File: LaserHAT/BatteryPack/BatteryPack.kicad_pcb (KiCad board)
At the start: 2 copper layers, 100 x 100 mm, 144 parts, among them J1 TYPE-C-31-M-12, J3 B4B-PH-K-S(LF)(SN), J5 S5B-XH-A-1(LF)(SN), J6 S5B-XH-A-1(LF)(SN), J7 XT60PW-M, J8 XT60PW-M, Q1 AO3401A, Q10 AO3400A, Q11 AO3400A, Q12 AO3400A, Q13 AO3401A, Q14 AO3400A, Q15 AO3400A, Q16 AO3400A, Q17 AO3400A, Q18 AO3400A, Q6 AO3401A, Q7 AO3400A, Q8 AO3400A, Q9 AO3400A, SW1 CAX-MTS203M-YB-10.6JL, U1 LM393DR2G, U10 HY2213-BB3A, U11 HY2213-BB3A, U12 HY2213-BB3A, U13 HY2213-BB3A, U14 LM393DR2G, U15 LM393DR2G, U16 CJ431, U2 LM393DR2G, U3 CJ431, U4 CH224A, U5 CN3704, U6 HY2213-BB3A, U7 HY2213-BB3A, U8 HY2213-BB3A, U9 HY2213-BB3A

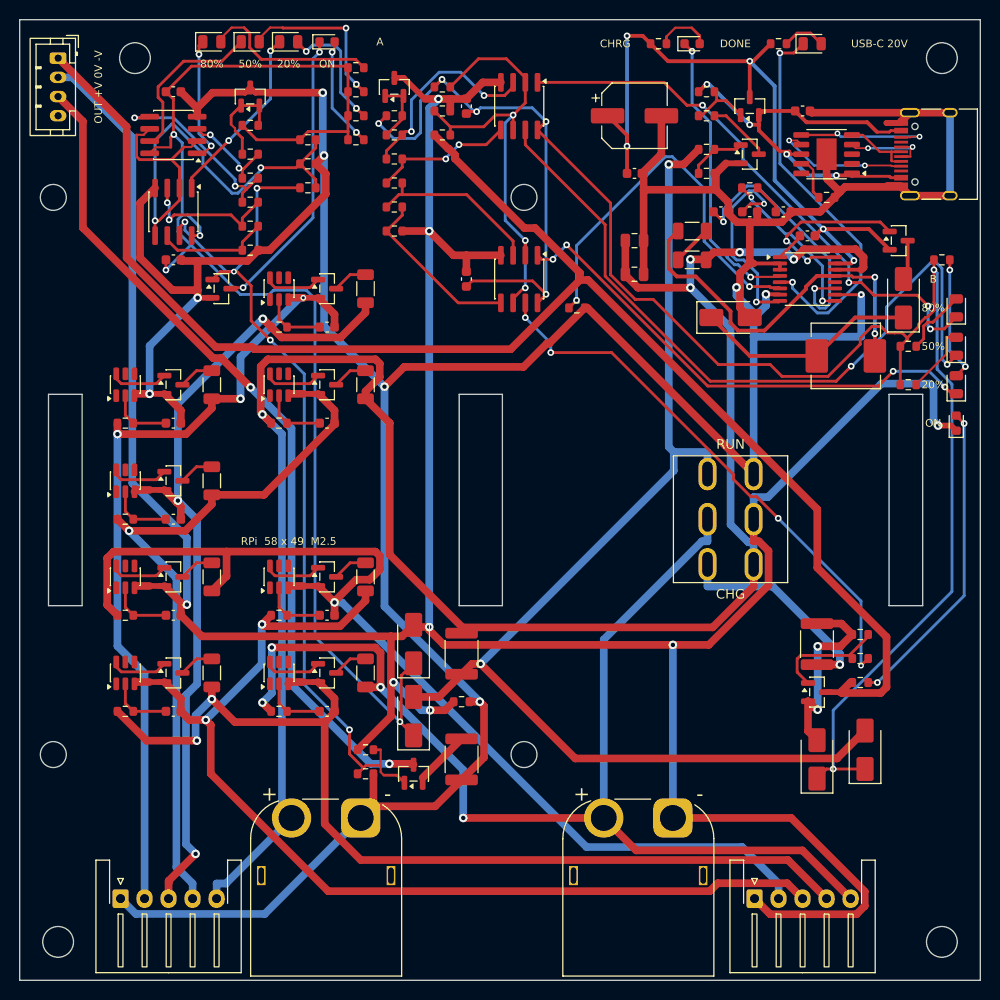
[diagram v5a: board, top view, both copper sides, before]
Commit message: BatteryPack rev D: packs in series, floating charger switched between them by a relay under an STM32F042, ON/OFF toggle, plug interlock, 0V pour
Rev C's parallel/series toggle made half the board jump by a pack voltage, needed a PTC link and an equalising rule, and left no single
reference.  Rev D keeps the packs in series for good (GND / 0V / +BATB), floats the whole charger on its own ground CGND and lets an
HFD2 relay under an STM32F042F4P6 (USB DFU, firmware/) connect it to pack A or pack B: "charge the lower pack" in 3-minute slots with
the CN3704 power-cycled at every reconnection, per-pack CHG / DONE LEDs.  MTS-202 ON/OFF toggle; +V is enabled only with the module's
plug in (J3 pin 4 strapped to 0V) because the module dies from +V / -V without 0V; an EL817 opto turns the outputs off while a brick
is in.  Gauge rails through P-FETs, ladder re-tuned for the undropped rail.

Layout mirror-symmetric about x = 50 with the Pi along the top edge (its USB-C / HDMI face flush, module over the top-right corner
above J3), the gauge LED columns paired in the centre (80 / 50 / 20 / ON / CHG / DONE), toggle and USB-C in the middle of the front,
relay front-right, PD sink front-left, charger island in the centre column under the Pi.  Freerouting + maze_route; back-side 0V
pour; DRC 0/0/0, path / sync 0, lcsc_check clean, fab outputs and renders regenerated.  Firmware compiles only with an ARM toolchain
(not present here); DFU on the TSSOP-20 and the relay's pick-up at 20 V are first-board checks (README).

Co-Authored-By: Claude Fable 5.1 <noreply@anthropic.com>
Claude-Session: https://claude.ai/code/session_018vgLizGzYPynnY93ajvoVA
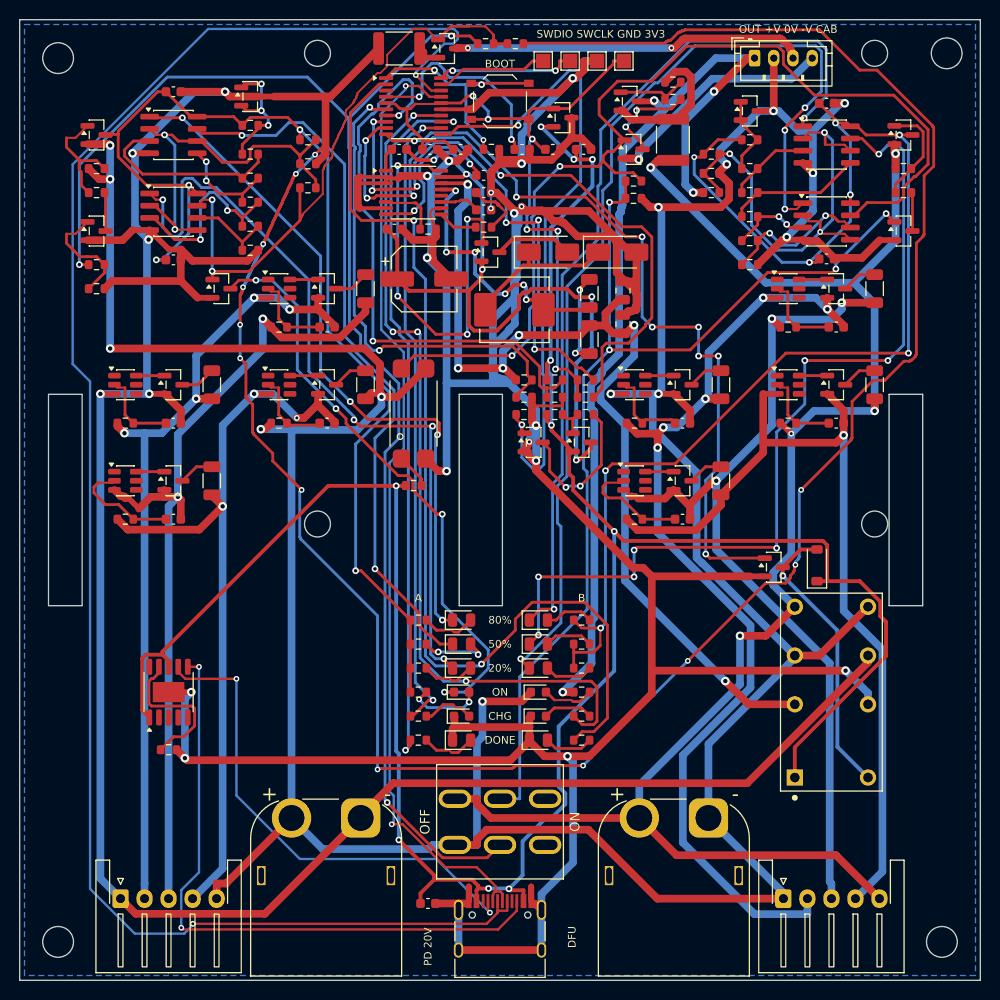
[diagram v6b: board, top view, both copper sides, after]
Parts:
- removed D15, D16, D5, D6: SS14, Diode_SMD:D_SMA
- removed F3: MF-MSMF110/24X-2, Fuse:Fuse_1812_4532Metric
- removed R30: 1M, Resistor_SMD:R_0603_1608Metric
- removed R41: 100k, Resistor_SMD:R_0603_1608Metric
- added C22: 1u, Capacitor_SMD:C_0603_1608Metric, F.Cu at (58.7, 13.5)
- added C23: 1u, Capacitor_SMD:C_0603_1608Metric, F.Cu at (55.5, 13.5)
- added C24: 100n, Capacitor_SMD:C_0603_1608Metric, F.Cu at (42.7, 13.5)
- added C25: 100n, Capacitor_SMD:C_0603_1608Metric, F.Cu at (45.9, 13.5)
- added C26: 100n, Capacitor_SMD:C_0603_1608Metric, F.Cu at (52.3, 13.5)
- added D17: KT-0603R, LED_SMD:LED_0603_1608Metric, F.Cu at (54.0, 72.5)
- added D18: KT-0805G, LED_SMD:LED_0805_2012Metric, F.Cu at (54.0, 75.0)
- added D19: 1N4148W, Diode_SMD:D_SOD-123, F.Cu at (83.0, 56.8)
- added K1: HFD2/024-M, battpack:Relay_HFD2, F.Cu at (84.5, 70.0)
- added Q19: 2N7002, Package_TO_SOT_SMD:SOT-23, F.Cu at (78.5, 57.0)
- added Q20: AO3401A, Package_TO_SOT_SMD:SOT-23, F.Cu at (8.00, 12.0)
- added Q21: 2N7002, Package_TO_SOT_SMD:SOT-23, F.Cu at (8.00, 22.0)
- added Q22: 2N7002, Package_TO_SOT_SMD:SOT-23, F.Cu at (63.9, 13.5)
- added Q23: AO3401A, Package_TO_SOT_SMD:SOT-23, F.Cu at (92.0, 12.0)
- added Q24: 2N7002, Package_TO_SOT_SMD:SOT-23, F.Cu at (92.0, 22.0)
- added R66: 1k, Resistor_SMD:R_0603_1608Metric, F.Cu at (41.5, 72.5)
- added R67: 470, Resistor_SMD:R_0603_1608Metric, F.Cu at (41.5, 75.0)
- added R68: 1k, Resistor_SMD:R_0603_1608Metric, F.Cu at (58.5, 72.5)
- added R69: 470, Resistor_SMD:R_0603_1608Metric, F.Cu at (58.5, 75.0)
- added R70: 10k, Resistor_SMD:R_0603_1608Metric, F.Cu at (49.1, 13.5)
- added R71: 100k, Resistor_SMD:R_0603_1608Metric, F.Cu at (52.5, 37.5)
- added R72: 18k, Resistor_SMD:R_0603_1608Metric, F.Cu at (52.5, 39.3)
- added R73: 100k, Resistor_SMD:R_0603_1608Metric, F.Cu at (55.7, 37.5)
- added R74: 18k, Resistor_SMD:R_0603_1608Metric, F.Cu at (55.7, 39.3)
- added R76: 10k, Resistor_SMD:R_0603_1608Metric, F.Cu at (41.0, 48.5)
- added R77: 100k, Resistor_SMD:R_0603_1608Metric, F.Cu at (8.00, 15.5)
- added R78: 100k, Resistor_SMD:R_0603_1608Metric, F.Cu at (8.00, 18.0)
- added R79: 100k, Resistor_SMD:R_0603_1608Metric, F.Cu at (8.00, 25.5)
- added R80: 100k, Resistor_SMD:R_0603_1608Metric, F.Cu at (8.00, 28.0)
- added R81: 1M, Resistor_SMD:R_0603_1608Metric, F.Cu at (63.9, 16.8)
- added R82: 1M, Resistor_SMD:R_0603_1608Metric, F.Cu at (63.9, 18.6)
- added R83: 100k, Resistor_SMD:R_0603_1608Metric, F.Cu at (92.0, 15.5)
- added R84: 100k, Resistor_SMD:R_0603_1608Metric, F.Cu at (92.0, 18.0)
- added SW2: TS-1187A-B-A-B, Button_Switch_SMD:SW_Push_1P1T_XKB_TS-1187A, F.Cu at (50.0, 8.50)
- added TP1: SWDIO, TestPoint:TestPoint_Pad_1.5x1.5mm, F.Cu at (54.5, 4.30)
- added TP2: SWCLK, TestPoint:TestPoint_Pad_1.5x1.5mm, F.Cu at (57.3, 4.30)
- added TP3: CGND, TestPoint:TestPoint_Pad_1.5x1.5mm, F.Cu at (60.1, 4.30)
- added TP4: +3V3, TestPoint:TestPoint_Pad_1.5x1.5mm, F.Cu at (62.9, 4.30)
- added U17: EL817S1(C)(TU)-F, battpack:EL817S1, F.Cu at (41.0, 41.0)
- added U18: TLV76033DBZR, Package_TO_SOT_SMD:SOT-23, F.Cu at (56.5, 10.2)
- added U19: STM32F042F4P6, Package_SO:TSSOP-20_4.4x6.5mm_P0.65mm, F.Cu at (41.0, 9.00)
- Q12: value AO3400A -> 2N7002
- R28, R29: value 15k -> 10k
- R4, R46: value 6.8k -> 6.2k
- SW1: value CAX-MTS203M-YB-10.6JL -> CAX-MTS202B2-BB-20.5JL; footprint battpack:SW_MTS-203 -> battpack:SW_MTS-202
- moved J1 93.7 mm to (50.0, 95.8), turned to 0 degrees
- moved C3 91.3 mm to (42.5, 92.0)
- moved R24 89.4 mm to (15.5, 76.0)
- moved U4 88.5 mm to (15.5, 70.0), turned to 90 degrees
- moved H7 86.8 mm to (89.0, 3.50)
- moved D10 81.2 mm to (46.0, 75.0)
- moved H8 78.0 mm to (31.0, 3.50)
- moved R40 77.6 mm to (51.6, 2.50)
- moved Q11 75.6 mm to (44.5, 3.00), turned to 0 degrees
- moved R39 74.6 mm to (48.5, 2.50)
- moved F2 74.3 mm to (39.5, 3.00), turned to 0 degrees
- moved D9 74.0 mm to (46.0, 72.5)
- moved J3 72.5 mm to (76.5, 4.00), turned to 0 degrees
- moved D1 69.1 mm to (46.0, 70.0)
- moved D2 67.6 mm to (46.0, 67.5)
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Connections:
- net /Q12_G renamed /CHG_EN
- C10 pad 2: GND -> CGND
- C11 pad 2: GND -> CGND
- C3 pad 2: GND -> CGND
- C5 pad 2: GND -> CGND
- C6 pad 2: GND -> CGND
- C7 pad 1: +BAT -> +CHG
- C7 pad 2: GND -> CGND
- C8 pad 1: +BAT -> +CHG
- C8 pad 2: GND -> CGND
- C9 pad 2: GND -> CGND
- D10 pad 1: /DONE -> CGND
- D8 pad 2: GND -> CGND
- D9 pad 1: /CHRG -> CGND
- F1 pad 1: +RUN -> +BATB
- J1 pad A1: GND -> CGND
- J1 pad A12: GND -> CGND
- J1 pad A6: Net-(U4-DP) -> /USB_DP
- J1 pad A7: Net-(U4-DM) -> /USB_DM
- J1 pad B1: GND -> CGND
- J1 pad B12: GND -> CGND
- J1 pad B6: Net-(U4-DP) -> /USB_DP
- J1 pad B7: Net-(U4-DM) -> /USB_DM
- J1 pad S1: GND -> CGND
- J3 pad 4: unconnected-(J3-Pin_4-Pad4) -> /CAB
- J5 pad 5: +BAT -> 0V
- J7 pad 2: +BAT -> 0V
- Q12 pad 2: GND -> CGND
- R2 pad 2: /CUT_OCB -> /Q22_D
- R24 pad 2: GND -> CGND
- R26 pad 2: +BAT -> +CHG
- R28 pad 1: VCHG -> +3V3
- R28 pad 2: Net-(D9-A) -> /CHRG
- R29 pad 1: VCHG -> +3V3
- R29 pad 2: Net-(D10-A) -> /DONE
- R34 pad 1: +BAT -> 0V
- R38 pad 1: +BAT -> 0V
- R39 pad 1: 0V -> /EN_A
- R42 pad 2: GND -> CGND
- RT1 pad 2: GND -> CGND
- SW1 pad 1: +BAT -> 0V
- SW1 pad 2: 0V -> /EN_A
- SW1 pad 3: GND -> unconnected-(SW1-B1-Pad3)
- SW1 pad 4: +RUN -> +BATB
- SW1 pad 5: +BATB -> /EN_B
- SW1 pad 6: +CHGB -> unconnected-(SW1-B2-Pad6)
- U15 pad 5: /THCUTB -> /VSB
- U15 pad 6: /VSB -> /THCUTB
- U15 pad 7: /CUT_OCB -> /ENB_G
- U4 pad 11: GND -> CGND
- U4 pad 4: Net-(U4-DP) -> unconnected-(U4-DP-Pad4)
- U4 pad 5: Net-(U4-DM) -> unconnected-(U4-DM-Pad5)
- U5 pad 10: GND -> CGND
- U5 pad 14: +BAT -> +CHG
- U5 pad 2: GND -> CGND
- U5 pad 3: GND -> CGND
- U5 pad 7: GND -> CGND
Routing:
- net CGND: track 0.00 -> 432.6 mm, vias 0 -> 17
- net VBUS: track 45.1 -> 256.7 mm, vias 4 -> 10
- net +BAT: track 211.3 -> 0.00 mm, vias 5 -> 0
- net /USB_DP: track 0.00 -> 180.9 mm, vias 0 -> 2
- net /EN_A: track 0.00 -> 151.0 mm, vias 0 -> 3
- net +CHGB: track 123.8 -> 0.00 mm, vias 2 -> 0
- net /EN_B: track 0.00 -> 108.2 mm, vias 0 -> 4
- net /ENB_G: track 0.00 -> 107.7 mm, vias 0 -> 2
- net /LED_DB: track 0.00 -> 105.8 mm, vias 0 -> 2
- net +CHG: track 0.00 -> 102.0 mm, vias 0 -> 6
- net /USB_DM: track 0.00 -> 100.7 mm, vias 0 -> 2
- net /LED_CB: track 0.00 -> 89.7 mm, vias 0 -> 4
- net GND: track 407.0 -> 495.3 mm, vias 9 -> 17
- net /RELAY: track 0.00 -> 80.0 mm, vias 0 -> 8
- net +3V3: track 0.00 -> 76.5 mm, vias 0 -> 6
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- added copper zone on B.Cu, net 0V
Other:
- board text added: "BOOT"
- board text added: "CHG"
- board text added: "DFU"
- board text added: "LaserHAT BatteryPack rev D"
- board text added: "OUT +V 0V -V CAB"
- board text added: "PD 20V"
- board text added: "SWDIO SWCLK GND 3V3"
- board text removed: "CHRG"
- board text removed: "LaserHAT BatteryPack rev C"
- board text removed: "OUT +V 0V -V"
- board text removed: "RPi 58 x 49 M2.5"
- board text removed: "USB-C 20V"

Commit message: BatteryPack rev D: audit fixes (relay, output socket, standby drain, relay pull-down, decoupling), re-routed
A layout audit found the home-made HFD2 relay footprint mirrored (the datasheet's PCB layout is a bottom view) with the coil
reversed, and the 24 V coil's 18 V pick-up had no margin on a 20 V bus.  Relay is now an Omron G6S-2 DC12 on KiCad's library
footprint, its 12 V coil fed through 680 R (R86), with R85 holding the driver off in reset / DFU and the flyback across the
coil.  The HFD2 footprint is corrected but unused.  Also from the audit: the pack-sense divider is 1M / 180k + 100n (it drew
140 uA from pack A whenever the brick was out and back-powered the MCU), J3 is a side-entry PH socket opening over the top
edge (a vertical header 2-7 mm inside the Pi's edge could not bend the cable in 3.5 mm), the BOOT button sits in the front
strip, the CH224A's 1 uF is beside it, the buck's freewheel diode and 1 uF are beside the switch, the VDDA cap is at its pin,
C7 / C8 are 22 uF 1206.  Re-placed and re-routed from scratch; DRC 0/0 with the 0V pour, path / sync 0, LCSC codes verified,
fab outputs and renders regenerated.

Co-Authored-By: Claude Fable 5.1 <noreply@anthropic.com>
Claude-Session: https://claude.ai/code/session_018vgLizGzYPynnY93ajvoVA
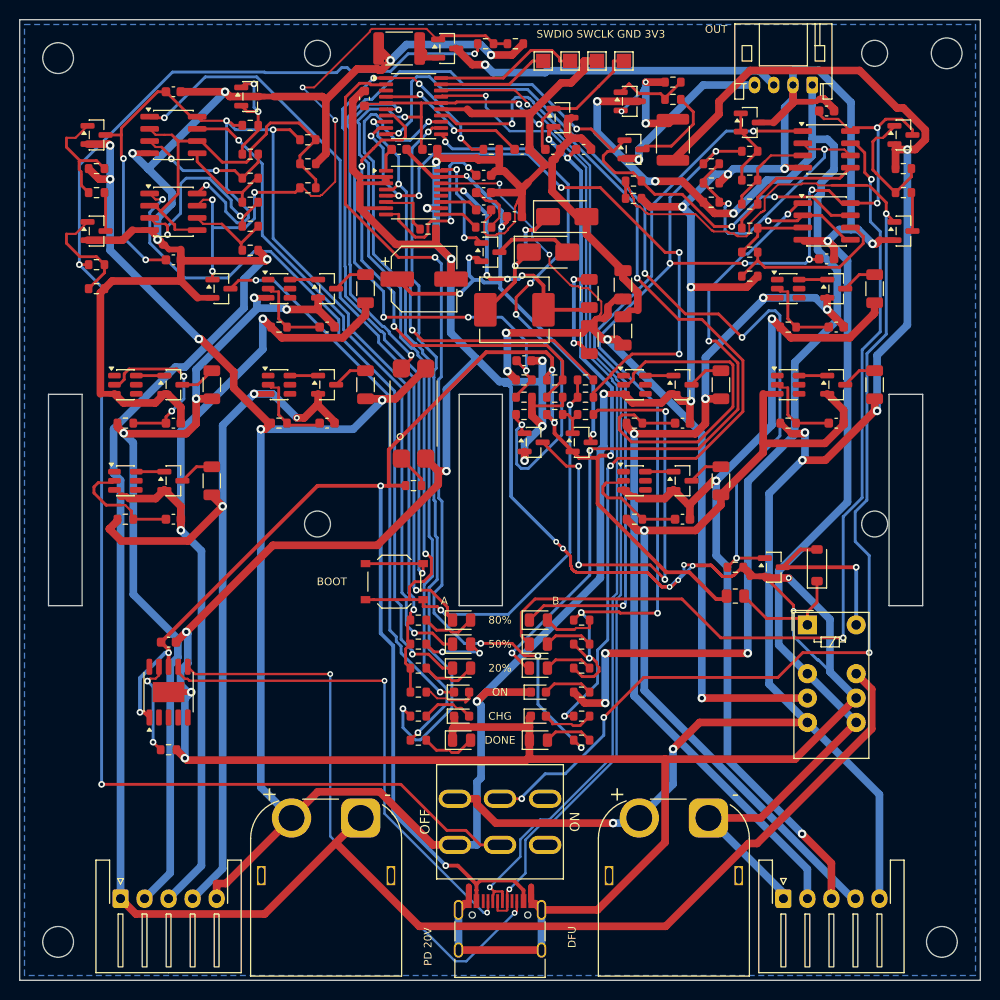
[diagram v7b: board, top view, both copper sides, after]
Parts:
- added C27: 100n, Capacitor_SMD:C_0603_1608Metric, F.Cu at (52.5, 35.5)
- added R85: 100k, Resistor_SMD:R_0603_1608Metric, F.Cu at (74.5, 57.0)
- added R86: 680, Resistor_SMD:R_0805_2012Metric, F.Cu at (74.5, 60.0)
- C7, C8: value 10u -> 22u; footprint Capacitor_SMD:C_0805_2012Metric -> Capacitor_SMD:C_1206_3216Metric
- J3: value B4B-PH-K-S(LF)(SN) -> S4B-PH-K-S(LF)(SN); footprint Connector_JST:JST_PH_B4B-PH-K_1x04_P2.00mm_Vertical -> Connector_JST:JST_PH_S4B-PH-K_1x04_P2.00mm_Horizontal
- K1: value HFD2/024-M -> G6S-2 DC12; footprint battpack:Relay_HFD2 -> Relay_THT:Relay_DPDT_Omron_G6S-2
- R71: value 100k -> 1M
- R72: value 18k -> 180k
- moved SW2 51.2 mm to (39.0, 58.5)
- moved C3 38.3 mm to (15.5, 64.8)
- moved C6 12.6 mm to (51.5, 20.5)
- moved C25 11.3 mm to (35.9, 8.20), turned to 90 degrees
- moved K1 7.43 mm to (82.0, 63.0), turned to 0 degrees
- moved J3 6.62 mm to (82.5, 6.80), turned to 180 degrees
- moved D8 6.38 mm to (57.0, 20.5)
- moved R45 1.20 mm to (76.0, 13.7)
- moved R46 1.20 mm to (76.0, 16.7)
- moved R47 1.20 mm to (76.0, 19.2)
- moved R48 1.20 mm to (76.0, 21.7)
- moved R49 1.20 mm to (76.0, 24.2)
- moved R50 1.20 mm to (76.0, 26.7)
- moved U16 1.20 mm to (76.0, 10.7)
- moved R51 1.00 mm to (72.0, 15.0)
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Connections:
- D19 pad 1: VBUS -> /RLY_P
- K1 pad 1: VBUS -> /RLY_P
- K1 pad 8: +BATB -> 0V
- K1 pad 9: 0V -> CGND
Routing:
- net GND: track 495.3 -> 310.6 mm, vias 17 -> 6
- net CGND: track 432.6 -> 515.5 mm, vias 17 -> 18
- net /USB_DP: track 180.9 -> 105.2 mm
- net +3V3: track 76.5 -> 145.3 mm
- net VBUS: track 256.7 -> 202.1 mm, vias 10 -> 9
- net /BOOT0: track 24.7 -> 78.7 mm, vias 3 -> 4
- net Net-(D12-K): track 107.0 -> 71.8 mm
- net /Q13_GD: track 15.9 -> 50.0 mm, vias 2 -> 4
- net Net-(Q6-G): track 43.2 -> 11.1 mm, vias 4 -> 2
- net Net-(U10-VDD): track 8.98 -> 38.6 mm
- net +OUT: track 100.0 -> 127.9 mm, vias 4 -> 6
- net /EN_B: track 108.2 -> 131.9 mm
- net VCHG: track 79.1 -> 58.4 mm
- net Net-(D14-K): track 91.7 -> 74.9 mm
- net /LED_DB: track 105.8 -> 90.8 mm, vias 2 -> 4
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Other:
- board text added: "OUT"
- board text removed: "OUT +V 0V -V CAB"

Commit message: BatteryPack rev D: second audit - K2 LINK relay isolates the charger while K1 moves, 33 uH, soft start, XT60 drills, JLC CPL rotations, HV clearance rules
A fresh, independent audit found that a single DPDT relay's poles are not
guaranteed to transfer together: with the charger island still tied to one
pack, the mismatched intermediate states put 33.6 V across the charger or short
its output capacitors through the contacts.  K2 (second G6S-2, both poles NO in
series with +CHG / CGND, PF1) now isolates the island while K1 moves; the
firmware opens K2, moves K1, closes K2, and keeps K2 open when idle, so the
island is off both packs at rest.

Also from the audit: L1 22 -> 33 uH (CN3704 table), C28 10 nF soft start on the
VBUS switch gate, R86/R88 680 R to 1206, XT60PW-M drills to Amass's 2025
drawing, CPL rotations corrected with the Fabrication Toolkit table
(make_fab.py wrote raw KiCad angles), 0.3 mm between Power-class nets on tracks
and 0.5 mm for the 33 V pairs (BatteryPack.kicad_dru), BRICK_MV 18 V, TP3 silk
CGND, RT1 moved clear of U5's bottom pins.  XT60 polarity documented as the
KiCad / hobby convention with the meter check kept as a first-board item.

Routing: autoroute.py now gives every pad of U5 / U19 a 0.2 mm escape stub and
takes locked pre-routes from route/preroute.json (the -V run along the top
edge); Freerouting + maze for the last ground links.  DRC 0/0 with the 0V pour,
path/sync 0, ERC 0, fab 175 placements / 54 BOM lines.

Co-Authored-By: Claude Fable 5.1 <noreply@anthropic.com>
Claude-Session: https://claude.ai/code/session_018vgLizGzYPynnY93ajvoVA
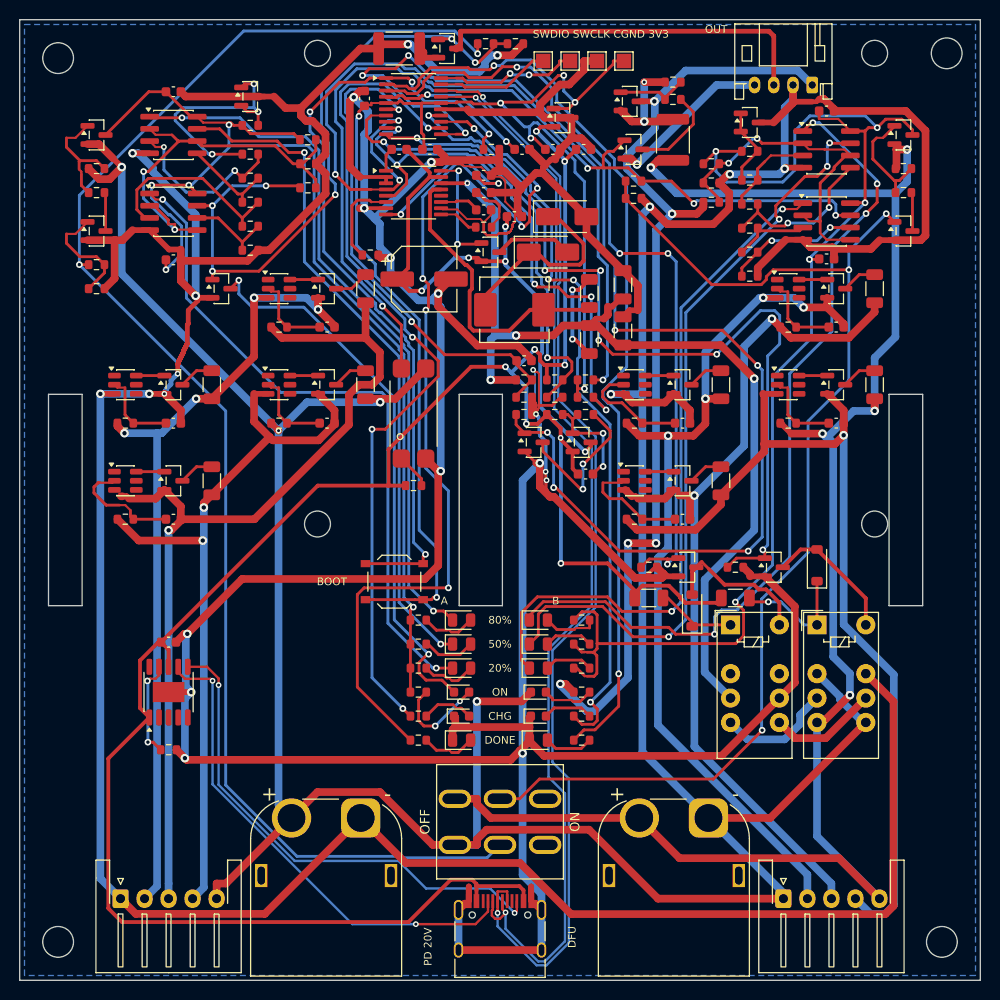
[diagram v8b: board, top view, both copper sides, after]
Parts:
- added C28: 10n, Capacitor_SMD:C_0603_1608Metric, F.Cu at (58.9, 47.3)
- added D20: 1N4148W, Diode_SMD:D_SOD-123, F.Cu at (70.0, 61.5)
- added K2: G6S-2 DC12, Relay_THT:Relay_DPDT_Omron_G6S-2, F.Cu at (74.0, 63.0)
- added Q25: 2N7002, Package_TO_SOT_SMD:SOT-23, F.Cu at (69.5, 57.0)
- added R87: 100k, Resistor_SMD:R_0603_1608Metric, F.Cu at (65.5, 57.0)
- added R88: 680, Resistor_SMD:R_1206_3216Metric, F.Cu at (65.5, 60.2)
- L1: value MWSA0603S-220MT -> MWSA0603S-330MT
- R86: footprint Resistor_SMD:R_0805_2012Metric -> Resistor_SMD:R_1206_3216Metric
- moved RT1 6.58 mm to (36.5, 24.5)
- moved K1 1.00 mm to (83.0, 63.0)
- moved R86 0.20 mm to (74.5, 60.2)
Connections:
- K1 pad 4: +CHG -> /CHG_K
- K1 pad 9: CGND -> /CGND_K
- U19 pad 3: unconnected-(U19-PF1-Pad3) -> /LINK
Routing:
- net /LINK: track 0.00 -> 83.3 mm, vias 0 -> 4
- net /CHG_EN: track 58.9 -> 134.3 mm, vias 4 -> 8
- net /CHRG: track 47.2 -> 85.0 mm, vias 3 -> 4
- net /Q13_GD: track 50.0 -> 16.5 mm, vias 4 -> 2
- net Net-(U10-VDD): track 38.6 -> 11.7 mm
- net +OUT: track 127.9 -> 102.3 mm, vias 6 -> 5
- net /LED_DA: track 81.1 -> 101.8 mm, vias 2 -> 6
- net VBUS: track 202.1 -> 222.8 mm, vias 9 -> 8
- net /LED_CB: track 100.6 -> 80.3 mm
- net /RLY2_K: track 0.00 -> 16.0 mm
- net /VREF: track 11.7 -> 25.6 mm, vias 2 -> 3
- net Net-(D13-K): track 94.2 -> 80.3 mm, vias 2 -> 4
- net Net-(D14-K): track 74.9 -> 87.5 mm, vias 2 -> 4
- net /LED_CA: track 75.0 -> 87.3 mm, vias 2 -> 4
- net /CHG_K: track 0.00 -> 12.1 mm
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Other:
- board text added: "SWDIO SWCLK CGND 3V3"
- board text removed: "SWDIO SWCLK GND 3V3"
